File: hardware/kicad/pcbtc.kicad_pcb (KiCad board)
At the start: 2 copper layers, 100 x 100 mm, 93 parts, among them J1 USB_C_Receptacle_USB2.0, J4 XT60, Q2 LMG5200, Q3 IPD50R380CE, Q4 LMG5200, SW1 Setup, T1 Transformer_1P_1S_0, U1 USBLC6-4SC6, U10 74LVC1G11, U11 USBLC6-4SC6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

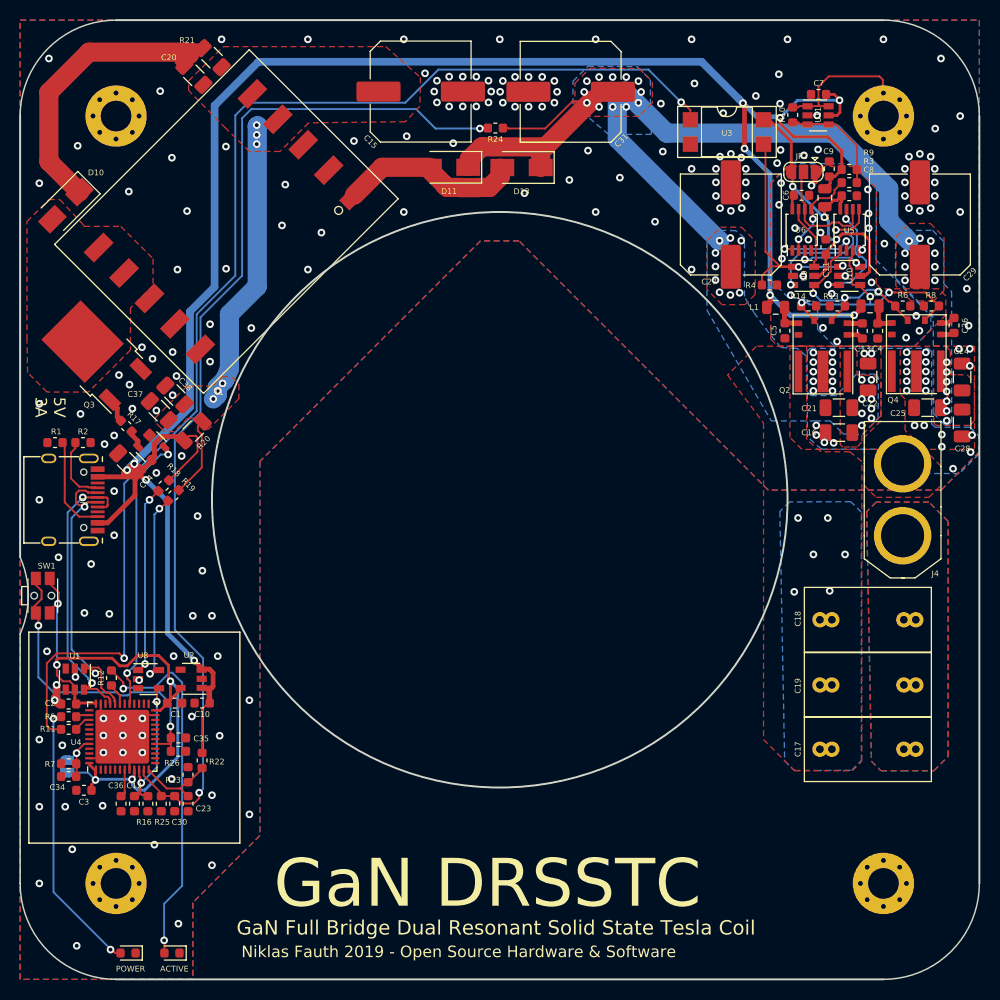
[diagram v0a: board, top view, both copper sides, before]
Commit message: Changed the STM32 QFN to an LQFP, easier to handle
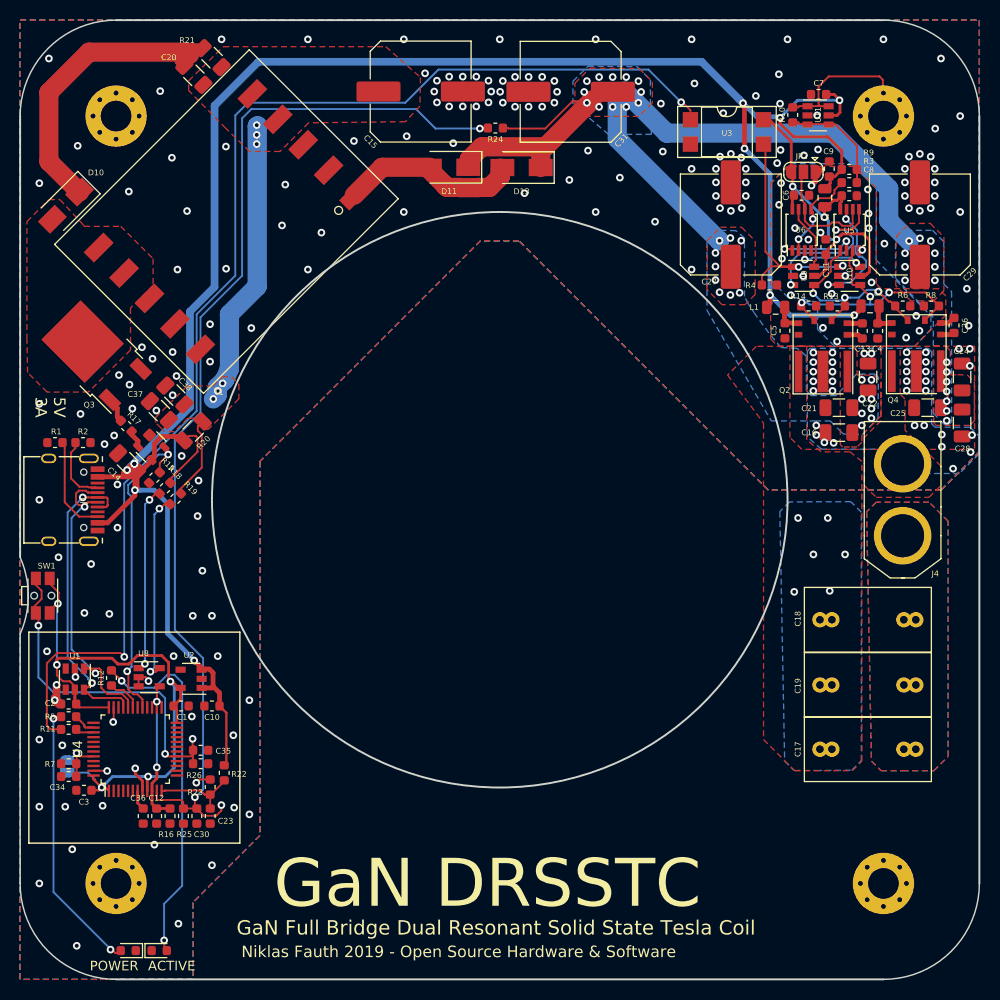
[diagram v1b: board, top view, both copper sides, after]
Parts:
- removed ACTIVE: FAULT, LED_SMD:LED_0603_1608Metric
- removed POWER: PWR, LED_SMD:LED_0603_1608Metric
- added FAULT1: FAULT, LED_SMD:LED_0603_1608Metric, F.Cu at (114.5, 127.0)
- added PWR1: PWR, LED_SMD:LED_0603_1608Metric, F.Cu at (111.3, 127.0)
- added R15: 5k1, Resistor_SMD:R_0603_1608Metric, F.Cu at (114.0, 77.7)
- C1, C10, C11, C2, C3, C36, C4, C5, C6, C7, C8, C9: value 0.1μF -> 100n
- C12: value 0.1μF -> 1n
- C14, C16, C21, C22, C24, C25, C28, C37, C38: value 220nF -> 10u
- C15: value 100uF -> 470u
- C23, C30, C34, C35: value 18p -> 1n
- C27, C29, C31: value 22u -> 220u
- D10: value SMA -> SS310
- D11, D13: value D -> SS310
- L1, L2, L3: value L_Core_Ferrite_Small -> CBW201209U600T
- R13, R14, R4, R6, R8: value 120 -> 1k
- R22, R23, R25: value 51k -> 5k1
- R24: value 1M -> 100k
- R5: value 1k -> 120
- U4: value STM32F072C8Ux -> STM32F072C8Tx; footprint Package_DFN_QFN:QFN-48-1EP_7x7mm_P0.5mm_EP5.6x5.6mm -> Package_QFP:LQFP-48_7x7mm_P0.5mm
- moved R22 2.65 mm to (121.3, 108.5)
- moved R23 2.65 mm to (119.8, 110.0)
- moved C23 2.65 mm to (119.8, 113.0)
- moved C30 2.65 mm to (118.4, 113.0)
- moved C36 2.65 mm to (112.8, 113.0)
- moved R16 2.65 mm to (115.6, 113.0)
- moved R25 2.65 mm to (117.0, 113.0)
- moved R26 2.65 mm to (118.8, 107.5)
- moved C12 2.65 mm to (114.2, 113.0)
- moved C35 2.65 mm to (118.8, 106.1)
- moved U4 1.87 mm to (112.0, 106.0)
- moved C10 1.07 mm to (120.0, 101.5)
- moved C1 0.74 mm to (116.8, 101.5)
- moved R19 0.41 mm to (116.2, 79.9)
- moved R18 0.30 mm to (115.1, 78.8)
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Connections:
- net FLYBACK renamed BOOST
- J1 pad A8: Net-(J1-PadA8) -> (no net)
- J1 pad B8: Net-(J1-PadB8) -> (no net)
- U1 pad 3: Net-(U1-Pad3) -> (no net)
- U1 pad 4: Net-(U1-Pad4) -> (no net)
- U2 pad 4: Net-(U2-Pad4) -> (no net)
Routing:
- net BOOST: track 29.3 -> 33.1 mm
- net Net-(C35-Pad1): track 33.7 -> 37.1 mm, vias 2 -> 3
- net U_OUT: track 109.9 -> 112.6 mm, vias 2 -> 3
- net GNDD: track 9.45 -> 12.1 mm, vias 200 -> 194
- net USB_DP: track 30.1 -> 31.7 mm
- net USB_DN: track 32.5 -> 34.1 mm
- net Net-(R12-Pad1): track 2.25 -> 3.67 mm
- net nRST: track 3.43 -> 2.08 mm
- net +5V: track 229.3 -> 230.6 mm
- net I_OUT: track 16.0 -> 14.7 mm
- net Net-(R11-Pad1): track 1.48 -> 2.69 mm
- net Net-(FAULT1-Pad2): track 38.6 -> 38.0 mm
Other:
- board text added: "ACTIVE"
- board text added: "POWER"

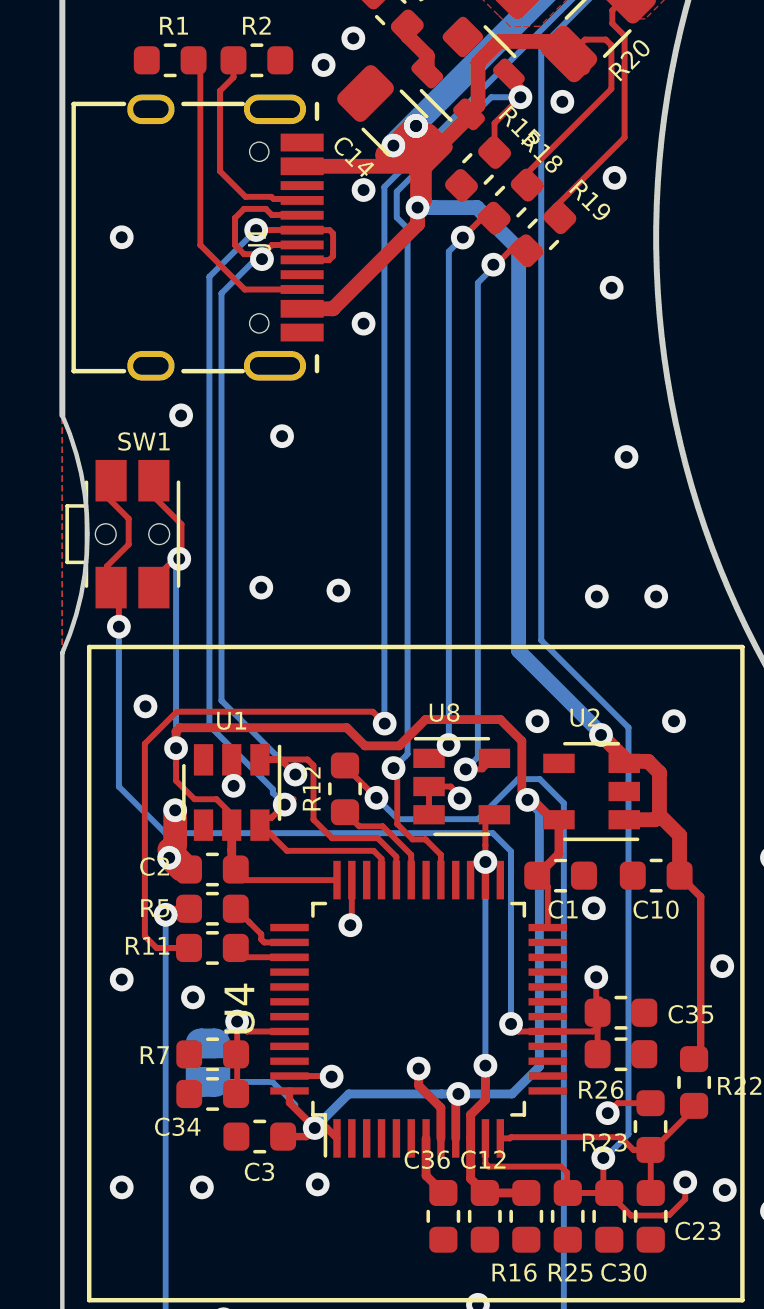
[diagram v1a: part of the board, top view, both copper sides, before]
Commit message: Fixed DRC errors
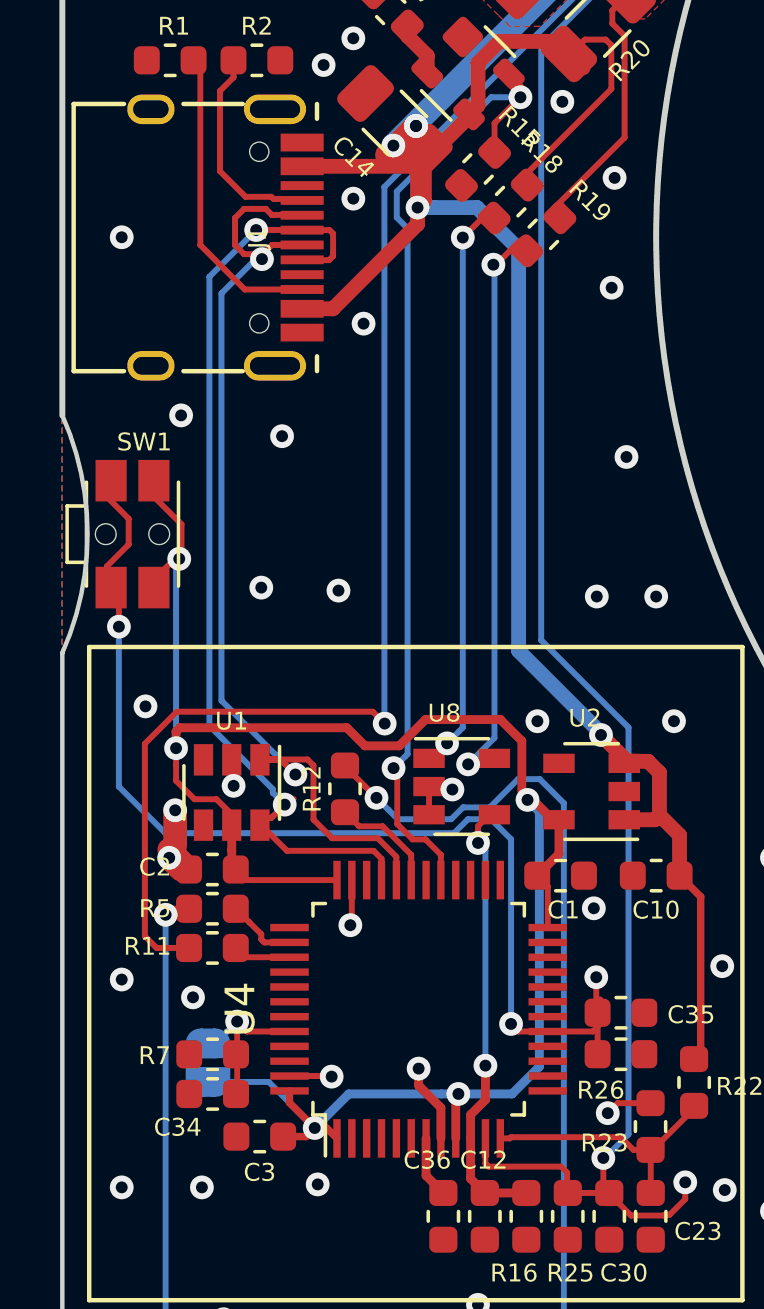
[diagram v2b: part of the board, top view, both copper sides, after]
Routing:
- net +3V3: track 66.2 -> 67.1 mm
- net Net-(C35-Pad1): track 37.1 -> 37.8 mm

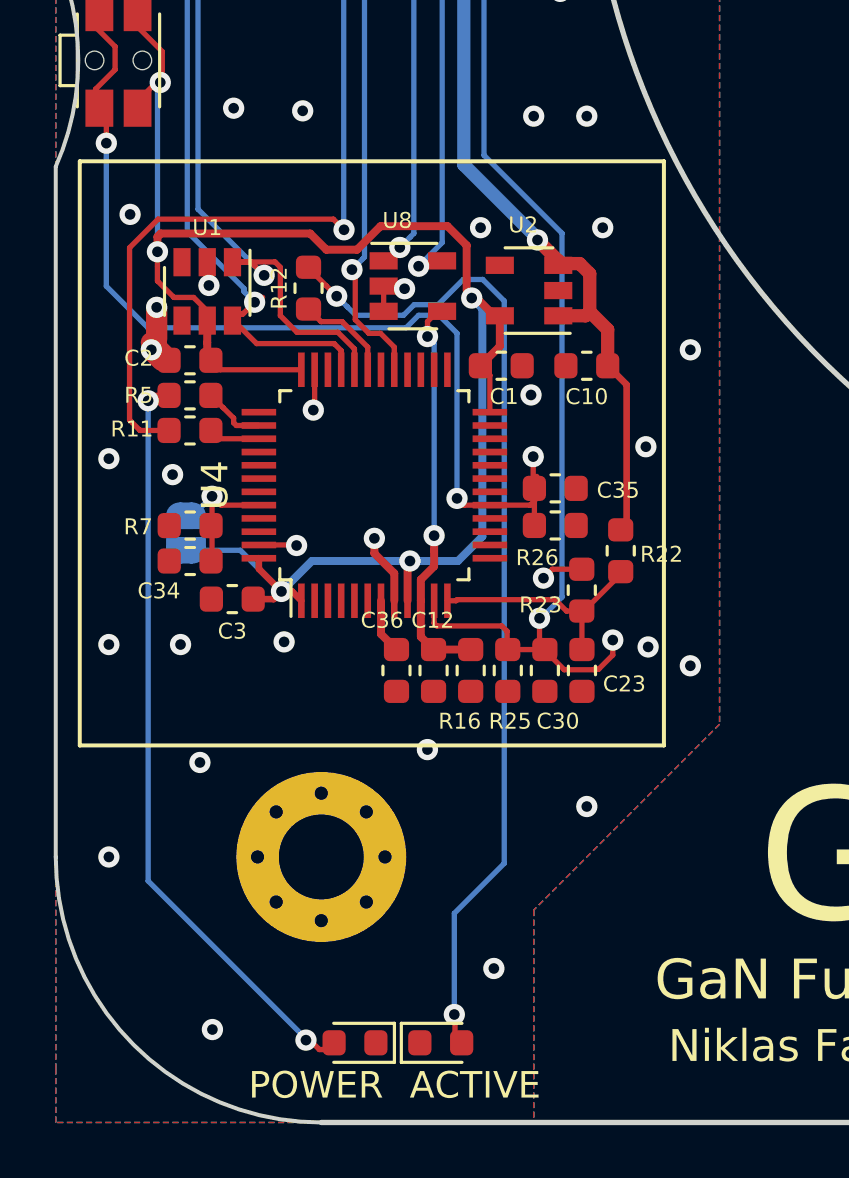
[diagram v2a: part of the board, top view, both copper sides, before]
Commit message: Previous component position caused some shorts to the can
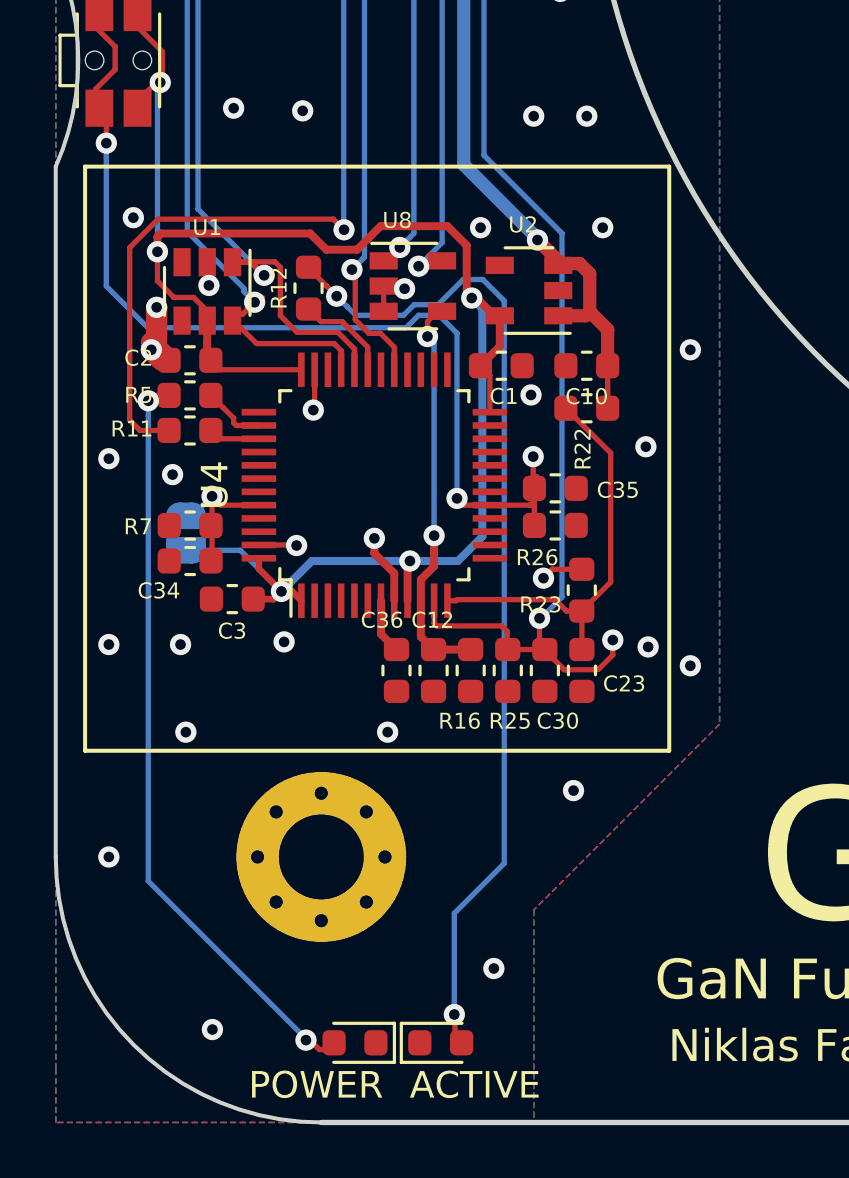
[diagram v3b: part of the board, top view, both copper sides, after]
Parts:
- moved R22 5.52 mm to (120.0, 103.1), turned to 180 degrees
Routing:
- net U_USB: track 8.74 -> 15.6 mm
- net +5V: track 230.6 -> 225.7 mm
